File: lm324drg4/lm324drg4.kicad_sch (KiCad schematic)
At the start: 0 parts

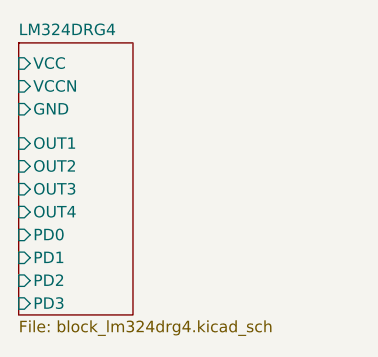
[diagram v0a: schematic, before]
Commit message: [Rushil] changed vccn to vee
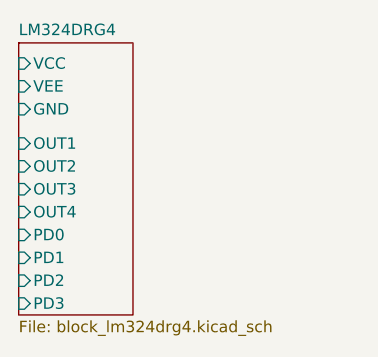
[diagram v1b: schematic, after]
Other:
- sheet LM324DRG4 ports: added VEE; removed VCCN
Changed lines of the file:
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@@
 			)
 		)
-		(pin "VCCN" input
+		(pin "VEE" input
 			(at 107.442 91.44 180)
 			(effects
